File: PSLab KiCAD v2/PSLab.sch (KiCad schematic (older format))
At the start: 69 parts, among them CON1 USB-MINI-B, P10 Analog, P12 5V, P13 MCLR, P2 PROG, P3 DIO, P4 V+/V-, P5 sen-cap, P6 I2C, P7 NRF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

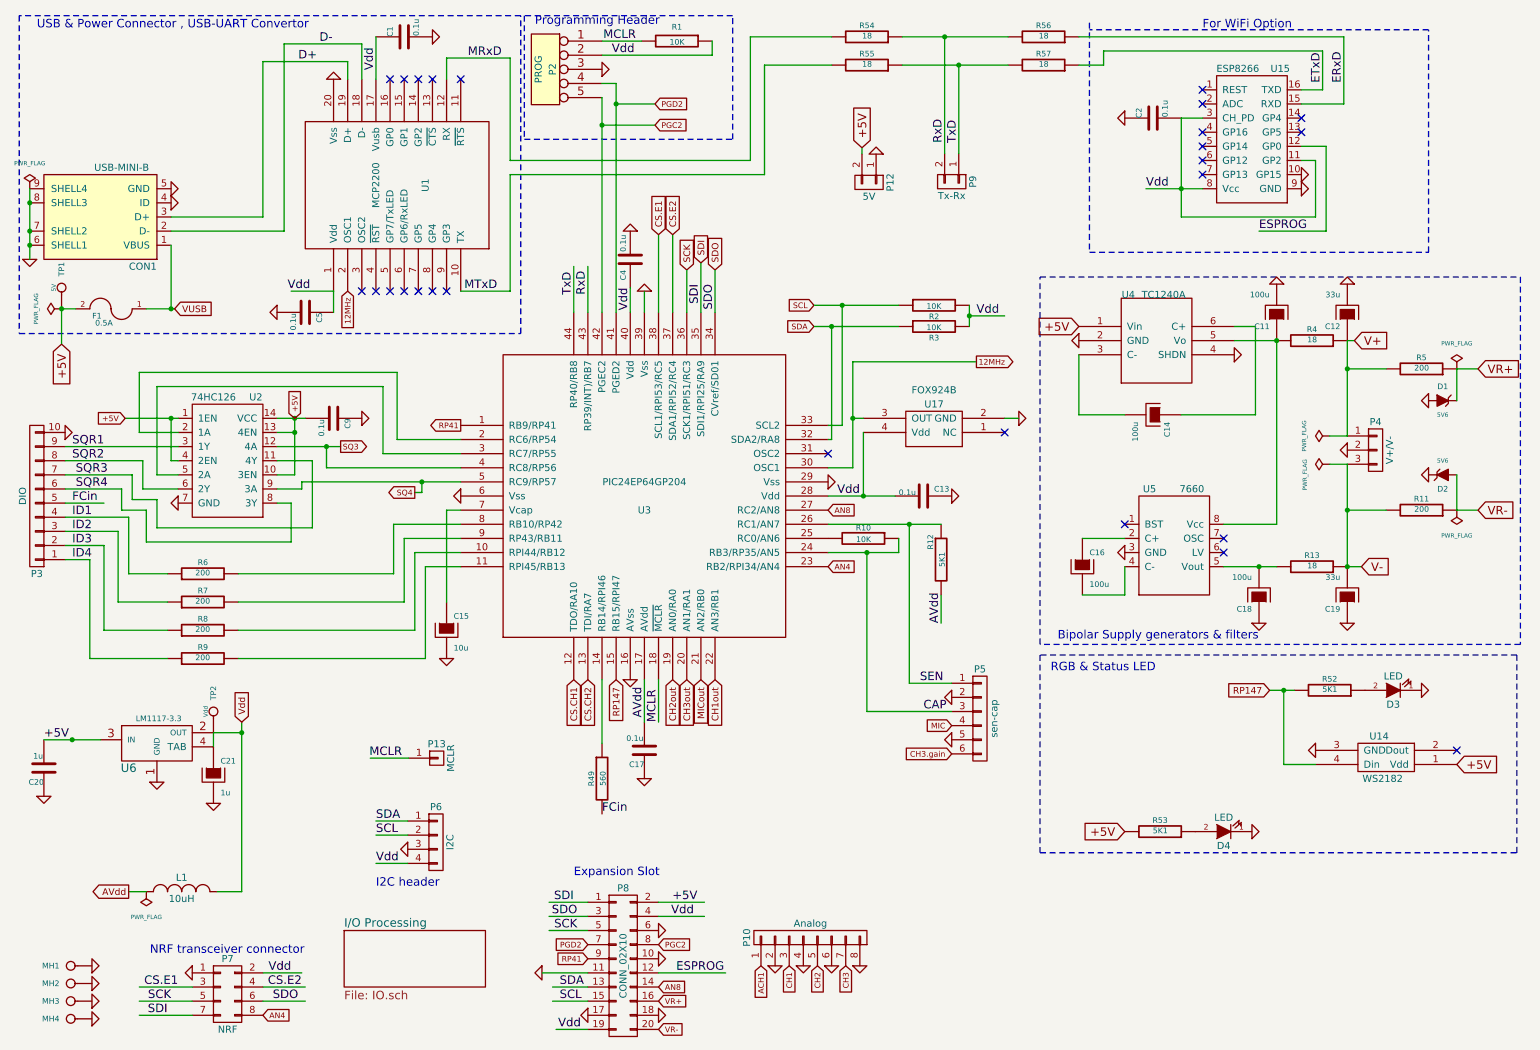
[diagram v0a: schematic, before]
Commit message: Fixed Electric rules
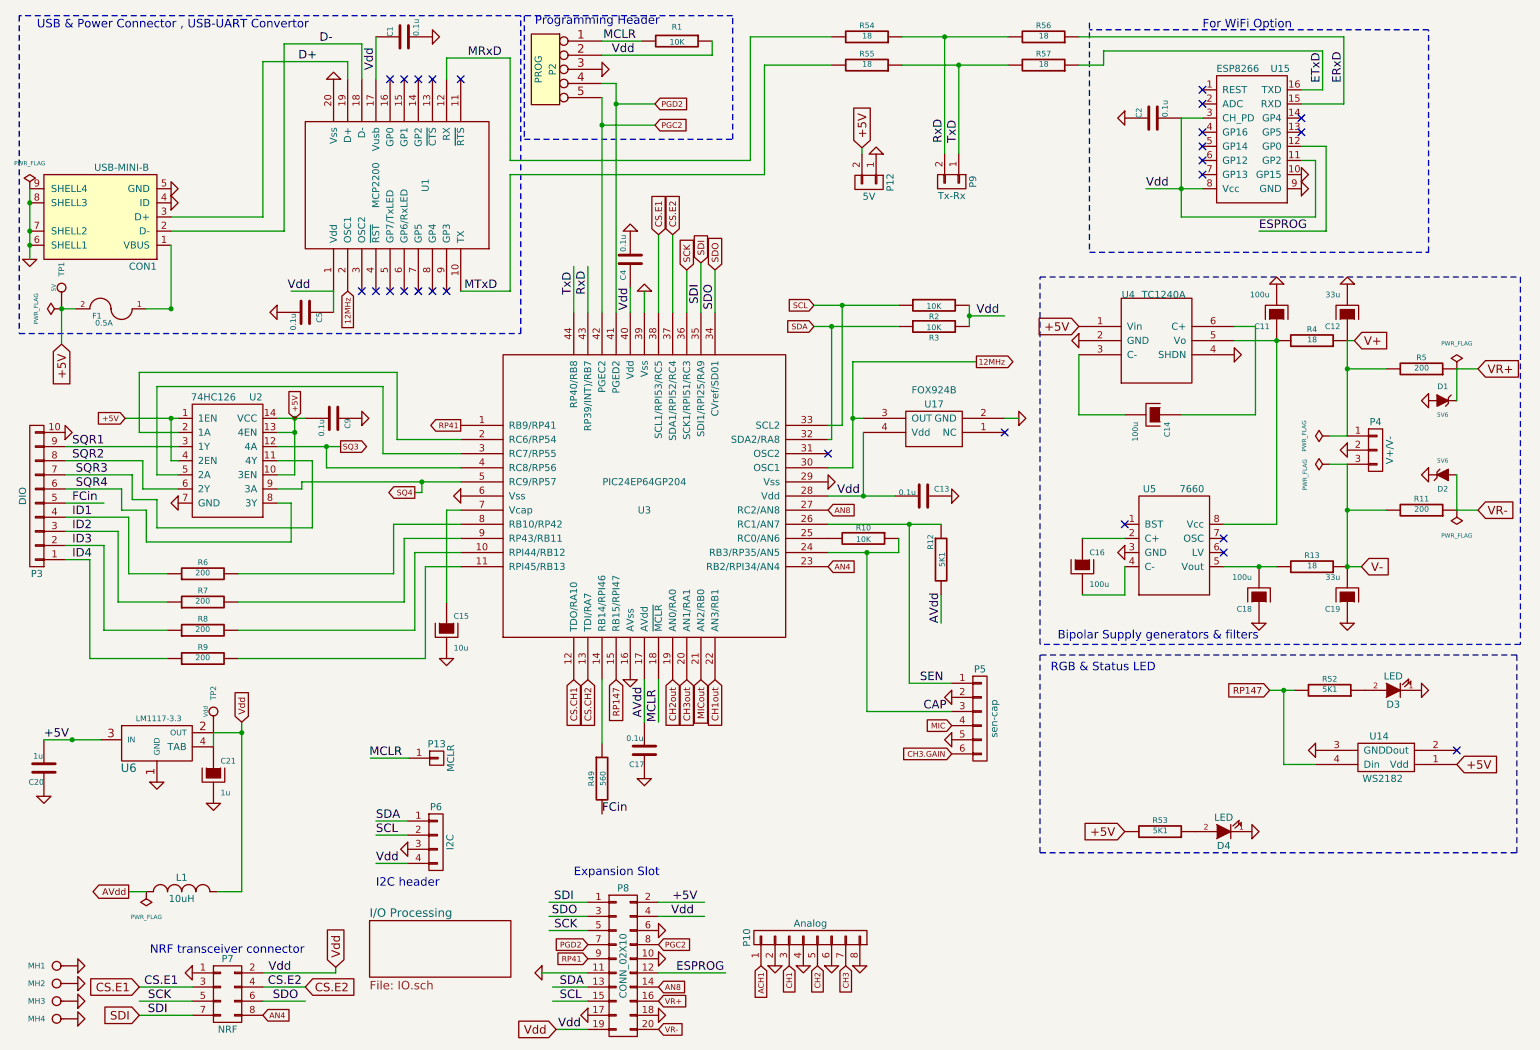
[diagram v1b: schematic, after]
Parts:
- U17: footprint _ -> Crystals:Crystal_SMD_EuroQuartz_MJ-4pin_5.0x3.2mm
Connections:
- net labels added: CH3.GAIN
- net labels removed: CH3.gain, VUSB
- wire segments 243 -> 216
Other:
- moved on the sheet: MH1, MH2, MH3, MH4

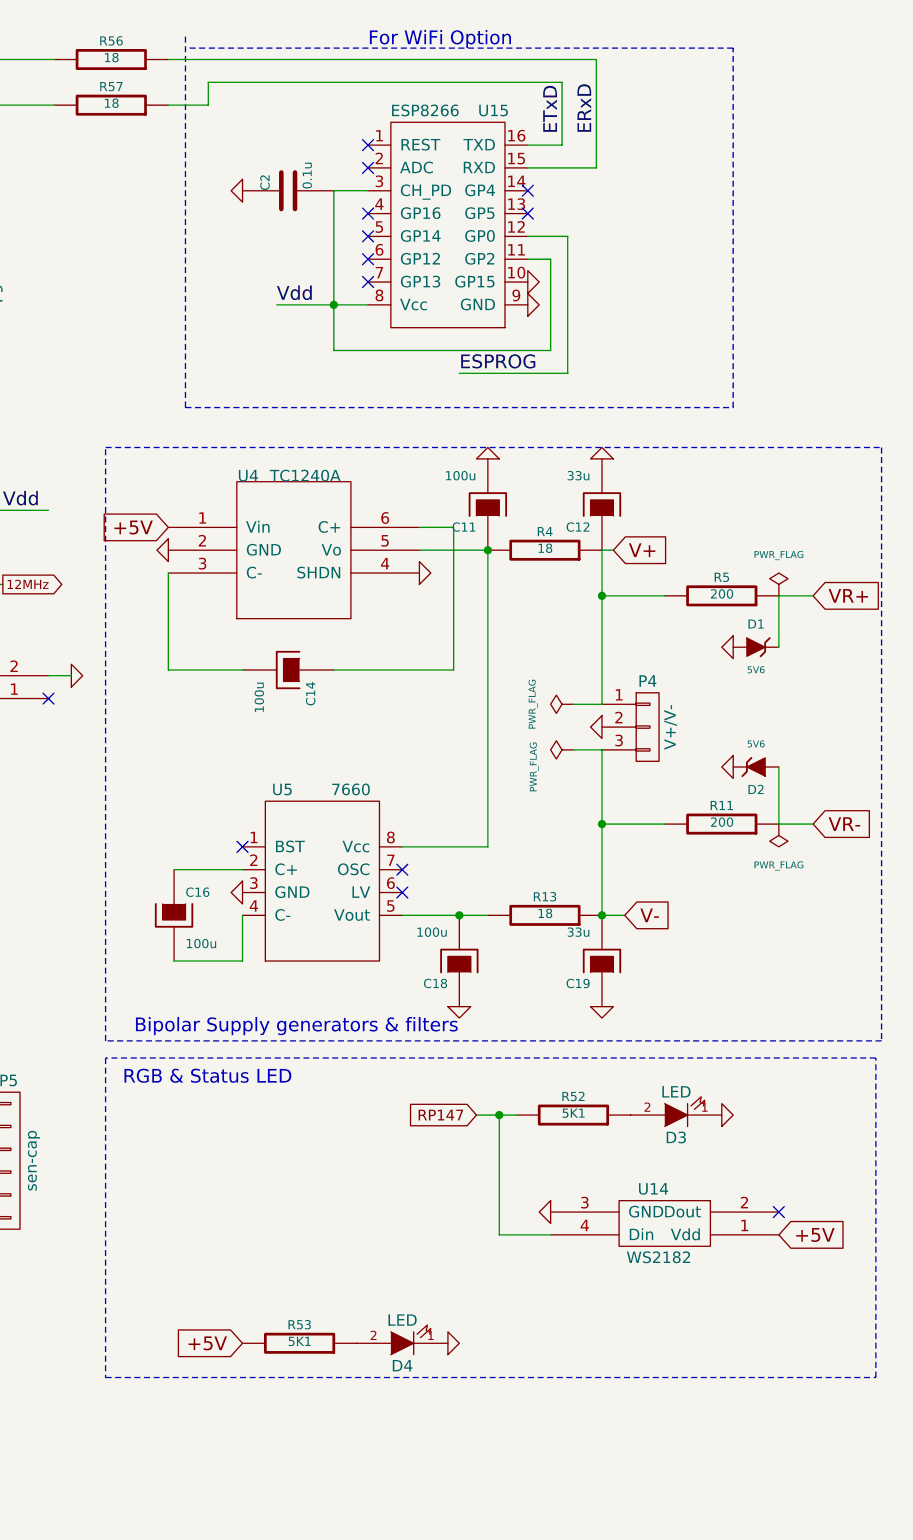
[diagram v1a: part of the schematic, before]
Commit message: Fix #19: Removed redundant LED foot print
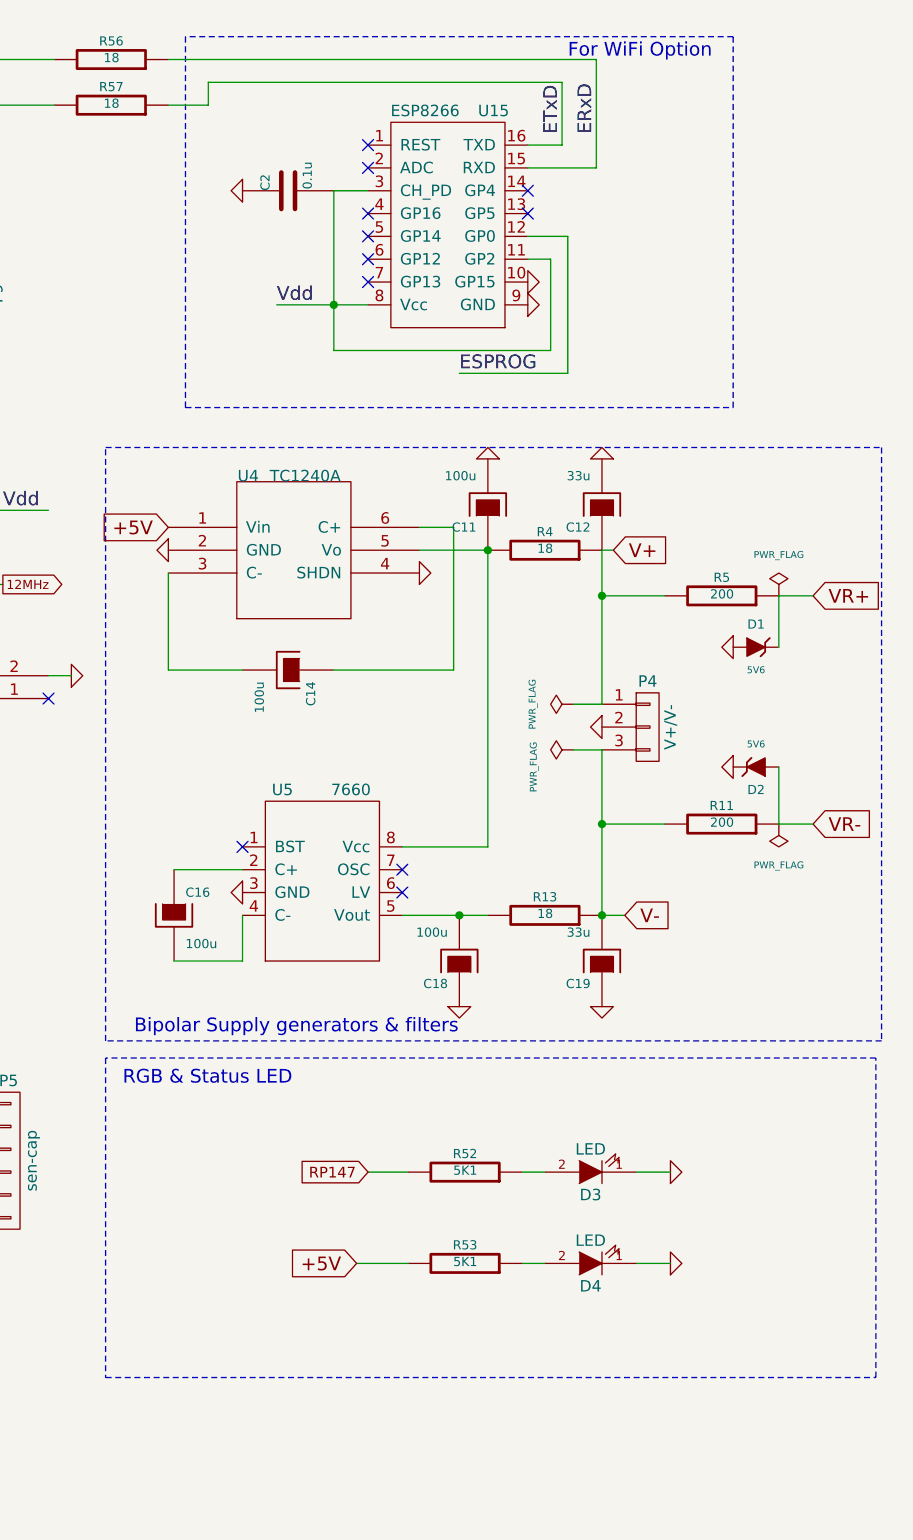
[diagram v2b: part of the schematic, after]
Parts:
- removed U14: WS2182, MyLib:SM5050, symbol WS2182
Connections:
- wire segments 216 -> 219
- no-connect marks 26 -> 25
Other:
- moved on the sheet: D3, D4, R52, R53
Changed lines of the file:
@@
 CH3.GAIN
-$Comp
-L WS2182 U14
-U 1 1 5574CE61
-P 10150 5700
-F 0 "U14" H 10150 5600 50  0000 C CNN
-F 1 "WS2182" H 10125 5900 50  0000 C CNN
-F 2 "MyLib:SM5050" H 10150 5900 50  0001 C CNN
-F 3 "DOCUMENTATION" H 10150 5500 50  0001 C CNN
-	1    10150 5700
-	-1   0    0    1
-$EndComp
-$Comp
-L GND-RESCUE-proto1 #PWR043
-U 1 1 5574EE9F
-P 9700 5700
-F 0 "#PWR043" H 9700 5700 30  0001 C CNN
-F 1 "GND" H 9700 5630 30  0001 C CNN
-F 2 "" H 9700 5700 60  0000 C CNN
-F 3 "" H 9700 5700 60  0000 C CNN
-	1    9700 5700
-	0    1    1    0
-$EndComp
-Text GLabel 10700 5800 2    60   Input ~ 0
-+5V
-NoConn ~ 10700 5700
 $Comp
 L CONN_01X04 P6
@@
 SCL
 $Comp
-L GND-RESCUE-proto1 #PWR044
+L GND-RESCUE-proto1 #PWR043
 U 1 1 55B40810
 P 3275 6400
-F 0 "#PWR044" H 3275 6400 30  0001 C CNN
+F 0 "#PWR043" H 3275 6400 30  0001 C CNN
 F 1 "GND" H 3275 6330 30  0001 C CNN
 F 2 "" H 3275 6400 60  0000 C CNN
@@
 PGC2
 $Comp
-L GND-RESCUE-proto1 #PWR045
+L GND-RESCUE-proto1 #PWR044
 U 1 1 55BA6E7D
 P 7125 5325
-F 0 "#PWR045" H 7125 5325 30  0001 C CNN
+F 0 "#PWR044" H 7125 5325 30  0001 C CNN
 F 1 "GND" H 7125 5255 30  0001 C CNN
 F 2 "" H 7125 5325 60  0000 C CNN
@@
 $EndComp
 $Comp
-L GND-RESCUE-proto1 #PWR046
+L GND-RESCUE-proto1 #PWR045
 U 1 1 55BAC428
 P 10500 3225
-F 0 "#PWR046" H 10500 3225 30  0001 C CNN
+F 0 "#PWR045" H 10500 3225 30  0001 C CNN
 F 1 "GND" H 10500 3155 30  0001 C CNN
 F 2 "" H 10500 3225 60  0000 C CNN
@@
 $EndComp
 $Comp
-L GND-RESCUE-proto1 #PWR047
+L GND-RESCUE-proto1 #PWR046
 U 1 1 55BACCF3
 P 10500 3750
-F 0 "#PWR047" H 10500 3750 30  0001 C CNN
+F 0 "#PWR046" H 10500 3750 30  0001 C CNN
 F 1 "GND" H 10500 3680 30  0001 C CNN
 F 2 "" H 10500 3750 60  0000 C CNN
@@
 AN8
 $Comp
-L GND-RESCUE-proto1 #PWR048
+L GND-RESCUE-proto1 #PWR047
 U 1 1 55BBD950
 P 5050 7175
-F 0 "#PWR048" H 5050 7175 30  0001 C CNN
+F 0 "#PWR047" H 5050 7175 30  0001 C CNN
 F 1 "GND" H 5050 7105 30  0001 C CNN
 F 2 "" H 5050 7175 60  0000 C CNN
@@
 $EndComp
 $Comp
-L PWR_FLAG #FLG049
+L PWR_FLAG #FLG048
 U 1 1 55BC0DD9
 P 10700 3000
-F 0 "#FLG049" H 10700 3095 30  0001 C CNN
+F 0 "#FLG048" H 10700 3095 30  0001 C CNN
 F 1 "PWR_FLAG" H 10700 3180 30  0000 C CNN
 F 2 "" H 10700 3000 60  0000 C CNN
@@
 $EndComp
 $Comp
-L PWR_FLAG #FLG050
+L PWR_FLAG #FLG049
 U 1 1 55BC113E
 P 10700 4000
-F 0 "#FLG050" H 10700 4095 30  0001 C CNN
+F 0 "#FLG049" H 10700 4095 30  0001 C CNN
 F 1 "PWR_FLAG" H 10700 4180 30  0000 C CNN
 F 2 "" H 10700 4000 60  0000 C CNN
@@
 MIC
 $Comp
-L GND-RESCUE-proto1 #PWR051
+L GND-RESCUE-proto1 #PWR050
 U 1 1 55C0E0F6
 P 7125 5625
-F 0 "#PWR051" H 7125 5625 30  0001 C CNN
+F 0 "#PWR050" H 7125 5625 30  0001 C CNN
 F 1 "GND" H 7125 5555 30  0001 C CNN
 F 2 "" H 7125 5625 60  0000 C CNN
@@
 Vdd
 $Comp
-L GND-RESCUE-proto1 #PWR052
+L GND-RESCUE-proto1 #PWR051
 U 1 1 55C20FB5
 P 5050 7575
-F 0 "#PWR052" H 5050 7575 30  0001 C CNN
+F 0 "#PWR051" H 5050 7575 30  0001 C CNN
 F 1 "GND" H 5050 7505 30  0001 C CNN
 F 2 "" H 5050 7575 60  0000 C CNN
@@
 NoConn ~ 2950 2450
 $Comp
-L GND-RESCUE-proto1 #PWR053
+L GND-RESCUE-proto1 #PWR052
 U 1 1 5564F446
 P 8350 1225
-F 0 "#PWR053" H 8350 1225 30  0001 C CNN
+F 0 "#PWR052" H 8350 1225 30  0001 C CNN
 F 1 "GND" H 8350 1155 30  0001 C CNN
 F 2 "" H 8350 1225 60  0000 C CNN
@@
 CH1
 $Comp
-L GND-RESCUE-proto1 #PWR054
+L GND-RESCUE-proto1 #PWR053
 U 1 1 55C57A66
 P 6275 7225
-F 0 "#PWR054" H 6275 7225 30  0001 C CNN
+F 0 "#PWR053" H 6275 7225 30  0001 C CNN
 F 1 "GND" H 6275 7155 30  0001 C CNN
 F 2 "" H 6275 7225 60  0000 C CNN
@@
 ACH1
 $Comp
-L PWR_FLAG #FLG055
+L PWR_FLAG #FLG054
 U 1 1 55EA2B09
 P 1425 6700
-F 0 "#FLG055" H 1425 6795 30  0001 C CNN
+F 0 "#FLG054" H 1425 6795 30  0001 C CNN
 F 1 "PWR_FLAG" H 1425 6880 30  0000 C CNN
 F 2 "" H 1425 6700 60  0000 C CNN
@@
 $EndComp
 $Comp
-L GND-RESCUE-proto1 #PWR056
+L GND-RESCUE-proto1 #PWR055
 U 1 1 55EB6CA8
 P 6475 7225
-F 0 "#PWR056" H 6475 7225 30  0001 C CNN
+F 0 "#PWR055" H 6475 7225 30  0001 C CNN
 F 1 "GND" H 6475 7155 30  0001 C CNN
 F 2 "" H 6475 7225 60  0000 C CNN
@@
 $EndComp
 $Comp
-L GND-RESCUE-proto1 #PWR057
+L GND-RESCUE-proto1 #PWR056
 U 1 1 55EB6D6D
 P 6075 7225
-F 0 "#PWR057" H 6075 7225 30  0001 C CNN
+F 0 "#PWR056" H 6075 7225 30  0001 C CNN
 F 1 "GND" H 6075 7155 30  0001 C CNN
 F 2 "" H 6075 7225 60  0000 C CNN
@@
 $EndComp
 $Comp
-L GND-RESCUE-proto1 #PWR058
+L GND-RESCUE-proto1 #PWR057
 U 1 1 55EB6E32
 P 5875 7225
-F 0 "#PWR058" H 5875 7225 30  0001 C CNN
+F 0 "#PWR057" H 5875 7225 30  0001 C CNN
 F 1 "GND" H 5875 7155 30  0001 C CNN
 F 2 "" H 5875 7225 60  0000 C CNN
@@
 	1    0    0    -1
 $EndComp
-Text GLabel 9375 5275 0    47   Input ~ 0
+Text GLabel 8900 5525 0    47   Input ~ 0
 RP147
 Text GLabel 6250 4400 2    40   Input ~ 0
@@
 $EndComp
 $Comp
-L GND-RESCUE-proto1 #PWR059
+L GND-RESCUE-proto1 #PWR058
 U 1 1 55EFED69
 P 850 3450
-F 0 "#PWR059" H 850 3450 30  0001 C CNN
+F 0 "#PWR058" H 850 3450 30  0001 C CNN
 F 1 "GND" H 850 3380 30  0001 C CNN
 F 2 "" H 850 3450 60  0000 C CNN
@@
 L LED-RESCUE-PSLab D3
 U 1 1 5660DA81
-P 10250 5275
-F 0 "D3" H 10250 5375 50  0000 C CNN
-F 1 "LED" H 10250 5175 50  0000 C CNN
-F 2 "MyLib:myPin_Header_Straight_1x02" H 10250 5275 60  0001 C CNN
-F 3 "" H 10250 5275 60  0000 C CNN
-	1    10250 5275
+P 9875 5525
+F 0 "D3" H 9875 5625 50  0000 C CNN
+F 1 "LED" H 9875 5425 50  0000 C CNN
+F 2 "MyLib:myPin_Header_Straight_1x02" H 9875 5525 60  0001 C CNN
+F 3 "" H 9875 5525 60  0000 C CNN
+	1    9875 5525
 	-1   0    0    1
 $EndComp
@@
 L R-RESCUE-proto1 R52
 U 1 1 5660DDAE
-P 9800 5275
-F 0 "R52" V 9880 5275 40  0000 C CNN
-F 1 "5K1" V 9807 5276 40  0000 C CNN
-F 2 "MyLib:R_0805" V 9730 5275 30  0001 C CNN
-F 3 "" H 9800 5275 30  0000 C CNN
-	1    9800 5275
+P 9325 5525
+F 0 "R52" V 9405 5525 40  0000 C CNN
+F 1 "5K1" V 9332 5526 40  0000 C CNN
+F 2 "MyLib:R_0805" V 9255 5525 30  0001 C CNN
+F 3 "" H 9325 5525 30  0000 C CNN
+	1    9325 5525
 	0    1    -1   0
 $EndComp
 $Comp
-L GND-RESCUE-proto1 #PWR060
+L GND-RESCUE-proto1 #PWR059
 U 1 1 5660E9DB
-P 10450 5275
-F 0 "#PWR060" H 10450 5275 30  0001 C CNN
-F 1 "GND" H 10450 5205 30  0001 C CNN
-F 2 "" H 10450 5275 60  0000 C CNN
-F 3 "" H 10450 5275 60  0000 C CNN
-	1    10450 5275
+P 10225 5525
+F 0 "#PWR059" H 10225 5525 30  0001 C CNN
+F 1 "GND" H 10225 5455 30  0001 C CNN
+F 2 "" H 10225 5525 60  0000 C CNN
+F 3 "" H 10225 5525 60  0000 C CNN
+	1    10225 5525
 	0    -1   -1   0
 $EndComp
@@
 L LED-RESCUE-PSLab D4
 U 1 1 56612B89
-P 9050 6275
-F 0 "D4" H 9050 6375 50  0000 C CNN
-F 1 "LED" H 9050 6175 50  0000 C CNN
-F 2 "MyLib:C_0805" H 9050 6275 60  0001 C CNN
-F 3 "" H 9050 6275 60  0000 C CNN
-	1    9050 6275
+P 9875 5925
+F 0 "D4" H 9875 6025 50  0000 C CNN
+F 1 "LED" H 9875 5825 50  0000 C CNN
+F 2 "MyLib:C_0805" H 9875 5925 60  0001 C CNN
+F 3 "" H 9875 5925 60  0000 C CNN
+	1    9875 5925
 	-1   0    0    1
 $EndComp
@@
 L R-RESCUE-proto1 R53
 U 1 1 56612DC3
-P 8600 6275
-F 0 "R53" V 8680 6275 40  0000 C CNN
-F 1 "5K1" V 8607 6276 40  0000 C CNN
-F 2 "MyLib:R_0805" V 8530 6275 30  0001 C CNN
-F 3 "" H 8600 6275 30  0000 C CNN
-	1    8600 6275
+P 9325 5925
+F 0 "R53" V 9405 5925 40  0000 C CNN
+F 1 "5K1" V 9332 5926 40  0000 C CNN
+F 2 "MyLib:R_0805" V 9255 5925 30  0001 C CNN
+F 3 "" H 9325 5925 30  0000 C CNN
+	1    9325 5925
 	0    1    -1   0
 $EndComp
 $Comp
-L GND-RESCUE-proto1 #PWR061
+L GND-RESCUE-proto1 #PWR060
 U 1 1 566130A1
-P 9250 6275
-F 0 "#PWR061" H 9250 6275 30  0001 C CNN
-F 1 "GND" H 9250 6205 30  0001 C CNN
-F 2 "" H 9250 6275 60  0000 C CNN
-F 3 "" H 9250 6275 60  0000 C CNN
-	1    9250 6275
+P 10225 5925
+F 0 "#PWR060" H 10225 5925 30  0001 C CNN
+F 1 "GND" H 10225 5855 30  0001 C CNN
+F 2 "" H 10225 5925 60  0000 C CNN
+F 3 "" H 10225 5925 60  0000 C CNN
+	1    10225 5925
 	0    -1   -1   0
 $EndComp
-Text GLabel 8350 6275 0    60   Input ~ 0
+Text GLabel 8850 5925 0    60   Input ~ 0
 +5V
 $Comp
@@
 $EndComp
 $Comp
-L GND-RESCUE-proto1 #PWR062
+L GND-RESCUE-proto1 #PWR061
 U 1 1 5667FFEB
 P 6590 1480
-F 0 "#PWR062" H 6590 1480 30  0001 C CNN
+F 0 "#PWR061" H 6590 1480 30  0001 C CNN
 F 1 "GND" H 6590 1410 30  0001 C CNN
 F 2 "" H 6590 1480 60  0000 C CNN
@@
 	1    0    0    -1
 $EndComp
-Text Notes 8900 600  0    60   ~ 0
+Text Notes 9775 650  0    60   ~ 0
 For WiFi Option
 Wire Wire Line
@@
 	5050 7275 5525 7275
 Wire Wire Line
-	9375 5275 9550 5275
-Wire Wire Line
-	9700 5800 9475 5800
-Wire Wire Line
-	9475 5800 9475 5275
-Connection ~ 9475 5275
+	8900 5525 9075 5525
 Wire Wire Line
 	9900 650  8025 650
@@
 	8100 2175 10500 2175
 Wire Notes Line
-	10500 2175 10500 600
-Wire Notes Line
-	10500 600  8100 600
+	10500 2175 10500 550
+Wire Notes Line
+	10500 550  8100 550
 Wire Notes Line
 	525  500  525  2750
@@
 Connection ~ 6425 3350
 $Comp
-L GND-RESCUE-proto1 #PWR063
+L GND-RESCUE-proto1 #PWR062
 U 1 1 591604FC
 P 7600 3350
-F 0 "#PWR063" H 7600 3350 30  0001 C CNN
+F 0 "#PWR062" H 7600 3350 30  0001 C CNN
 F 1 "GND-RESCUE-proto1" H 7600 3280 30  0001 C CNN
 F 2 "" H 7600 3350 60  0000 C CNN
@@
 Wire Wire Line
 	1600 2575 1425 2575
+Wire Wire Line
+	8850 5925 9075 5925
+Wire Wire Line
+	9575 5925 9675 5925
+Wire Wire Line
+	10225 5925 10075 5925
+Wire Wire Line
+	10075 5525 10225 5525
+Wire Wire Line
+	9675 5525 9575 5525
 $EndSCHEMATC
